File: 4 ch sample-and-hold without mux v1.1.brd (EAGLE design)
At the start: 17.6 x 10 mm, 8 parts, among them IC5 TL084CPWR

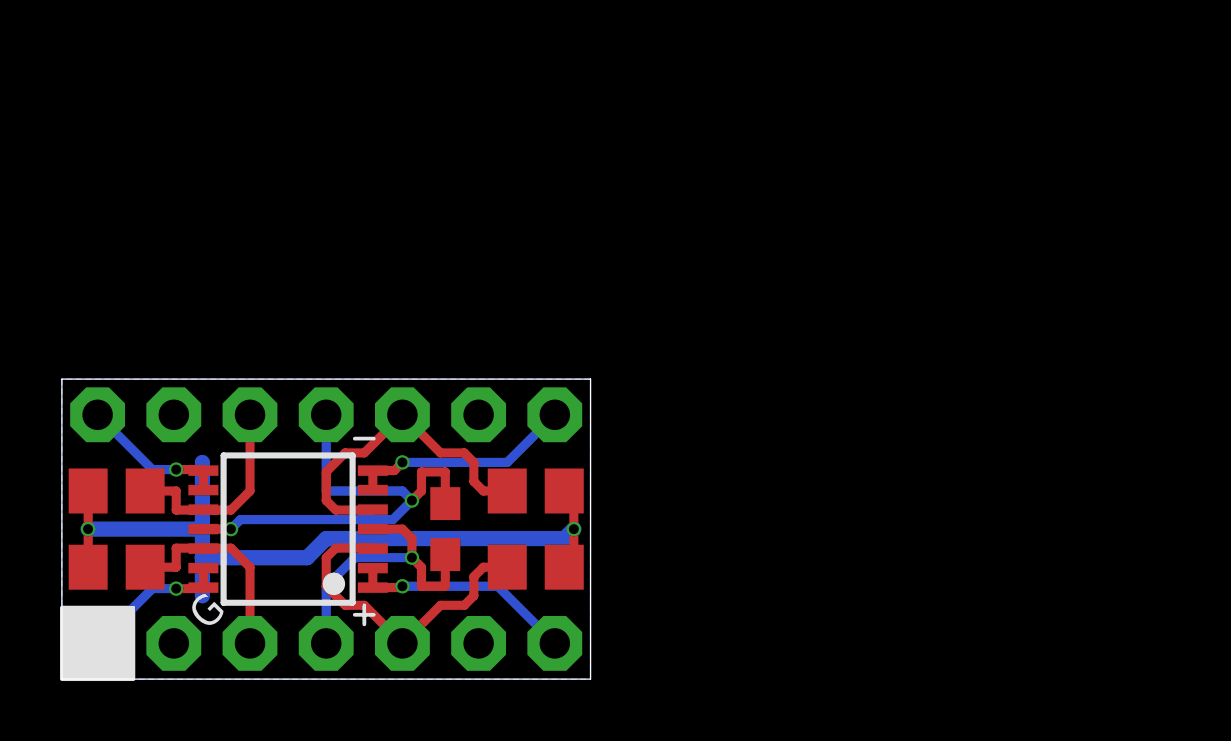
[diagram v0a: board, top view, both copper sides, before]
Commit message: Fixed error in silk screen
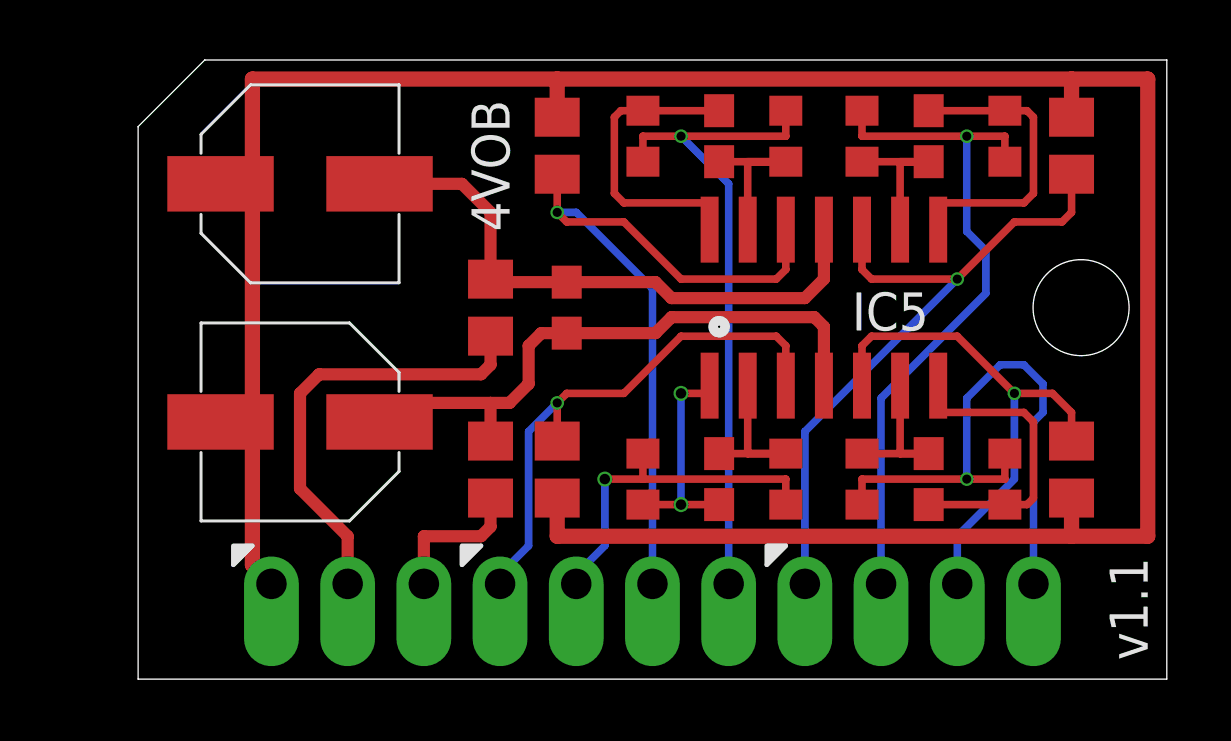
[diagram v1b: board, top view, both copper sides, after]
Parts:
- removed 1-7, 8-14: MA07-1JN, joakim:MA07N-1J
- added C2, C3: 22uF 25V, joakim-jclpcb:CAPAE660X610N
- added C36, C37, C38, C39: 330pF, resistor:C0603
- added R1, R2: 100R, rcl:R0805
- added R27, R29, R31, R33: 1k, resistor:R0603
- added R28, R30, R32, R34: 100R, resistor:R0603
- added SV1, SV2: (no value), joakim:SIP-PIN04-1J
- added SV3: (no value), joakim:SIP-PIN03-1J
- added U$1: (no value), joakim:XONIK_LOGO_20
- IC5: value TL084CPWR -> TL074D; device joakim:TSSOP14J -> linear:SO14
- moved C27 33.8 mm to (33.7, 17.8), turned to 270 degrees
- moved C26 20.3 mm to (16.5, 17.8), turned to 270 degrees
- moved IC5 19.3 mm to (25.4, 12.4), turned to 0 degrees
- moved C28 17.9 mm to (33.7, 6.99), turned to 90 degrees
- moved C31 8.42 mm to (16.8, 12.4)
- moved C29 3.33 mm to (16.5, 6.99), turned to 90 degrees
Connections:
- new net N$33: C39.1, IC5.1, R34.1
- new net N$34: C39.2, IC5.2, R33.1
- new net N$35: C38.1, IC5.7, R32.1
- new net N$36: C38.2, IC5.6, R31.1
- new net N$37: C37.1, IC5.8, R30.1
- new net N$38: C36.1, IC5.14, R28.1
- new net N$39: C37.2, IC5.9, R29.1
- new net N$40: C36.2, IC5.13, R27.1
- new net V+: R2.2, SV3.3
- new net V-: R1.2, SV3.2
- net +15V: now also C3.1, R2.1; no longer 1-7.4
- net -15V: now also C2.2, R1.1; no longer 8-14.4
- net AGND: now also C2.1, C3.2, SV3.1; no longer 1-7.2
- net IN1: now also C29.2, IC5.3, SV1.1; no longer 1-7.3, C26.2, IC5.12
- net IN2: now also C26.2, IC5.12, SV1.3; no longer 1-7.5, C29.2, IC5.3
- net IN3: now also C27.2, IC5.10, SV2.1; no longer 8-14.3, C28.2, IC5.5
- net IN4: now also C28.2, IC5.5, SV2.3; no longer 8-14.5, C27.2, IC5.10
- net OUT1: now also R33.2, R34.2, SV1.2; no longer 1-7.1, IC5.13, IC5.14
- net OUT2: now also R27.2, R28.2, SV1.4; no longer 1-7.7, IC5.1, IC5.2
- net OUT3: now also R29.2, R30.2, SV2.2; no longer 8-14.1, IC5.6, IC5.7
- net OUT4: now also R31.2, R32.2, SV2.4; no longer 8-14.7, IC5.8, IC5.9
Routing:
- net AGND: track 26.4 -> 89.1 mm, vias 2 -> 0
- net OUT3: track 7.49 -> 23.1 mm
- net V-: track 0.00 -> 14.7 mm
- net OUT2: track 7.52 -> 22.0 mm
- net IN2: track 10.9 -> 25.3 mm, vias 0 -> 1
- net OUT4: track 4.95 -> 19.2 mm
- net IN3: track 10.9 -> 22.9 mm, vias 0 -> 1
- net IN1: track 6.95 -> 18.1 mm, vias 0 -> 1
- net IN4: track 6.95 -> 17.6 mm, vias 0 -> 1
- net N$37: track 0.00 -> 10.3 mm
- net N$38: track 0.00 -> 10.3 mm
- net N$35: track 0.00 -> 10.3 mm
- net +15V: track 10.2 -> 20.4 mm, vias 1 -> 0
- net N$33: track 0.00 -> 7.46 mm, vias 0 -> 2
- net OUT1: track 4.95 -> 11.6 mm
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- removed copper zone on layer 16, net AGND
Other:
- board size 17.6 x 10 mm -> 34.3 x 20.6 mm
- board text added: "+15v"
- board text added: "-15v"
- board text added: "1"
- board text added: "2"
- board text added: "3"
- board text added: "4"
- board text added: "4 ch. CV buffer"
- board text added: "AGND"
- board text added: "IN"
- board text added: "OUT"
- board text added: "v1.1"
- board text removed: "G"
- board text removed: "S&H v1.0"
